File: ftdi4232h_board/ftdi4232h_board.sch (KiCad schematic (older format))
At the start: 20 parts

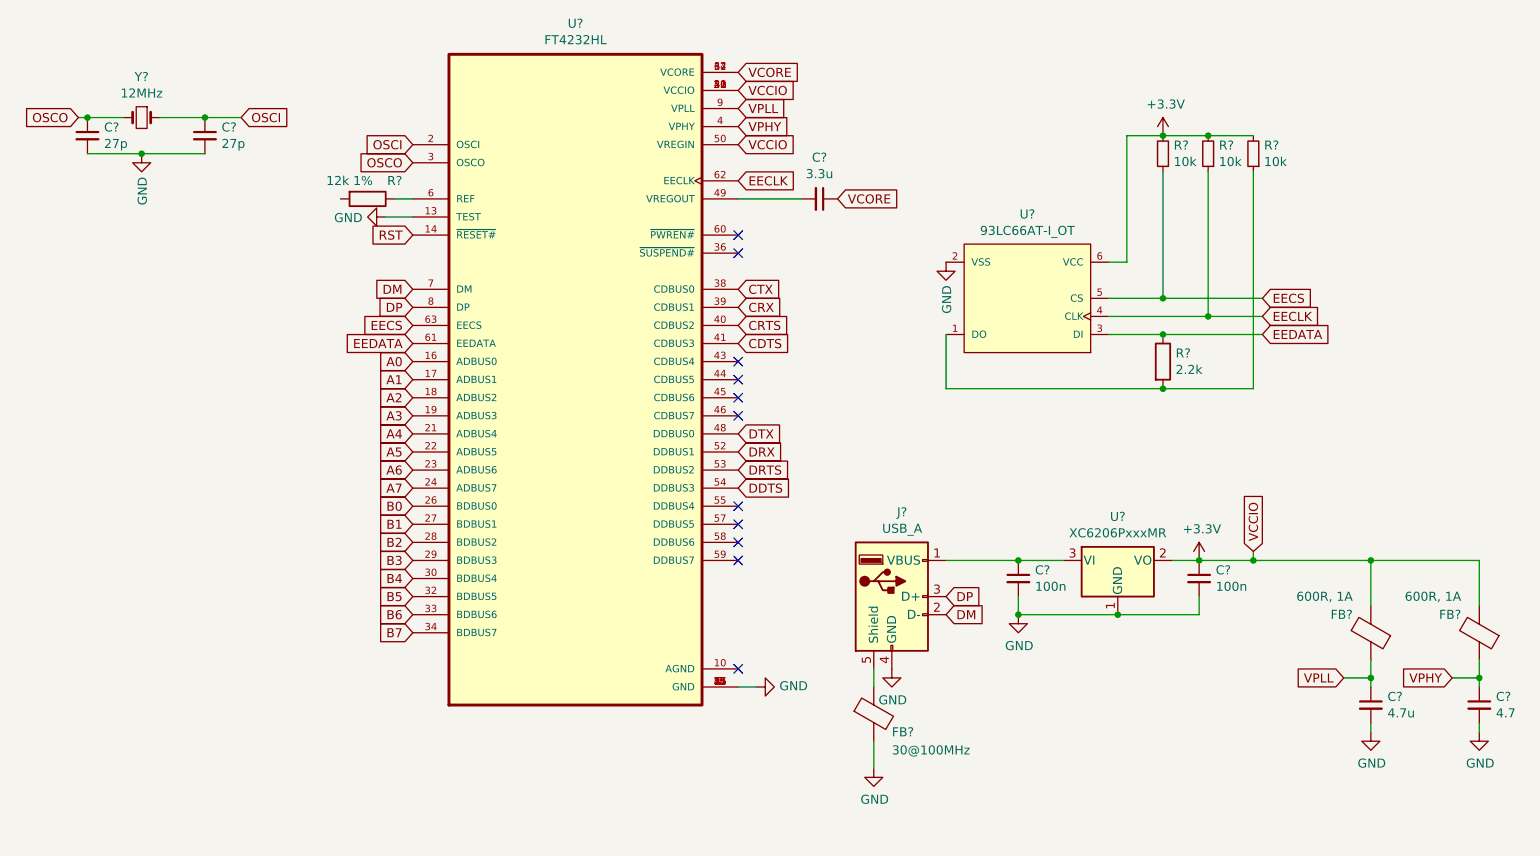
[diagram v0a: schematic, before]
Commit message: Use TPD2E2U06 as ESD protection for USB
The PCB design seems much more natural for USB using this IC compared to
alternatives.
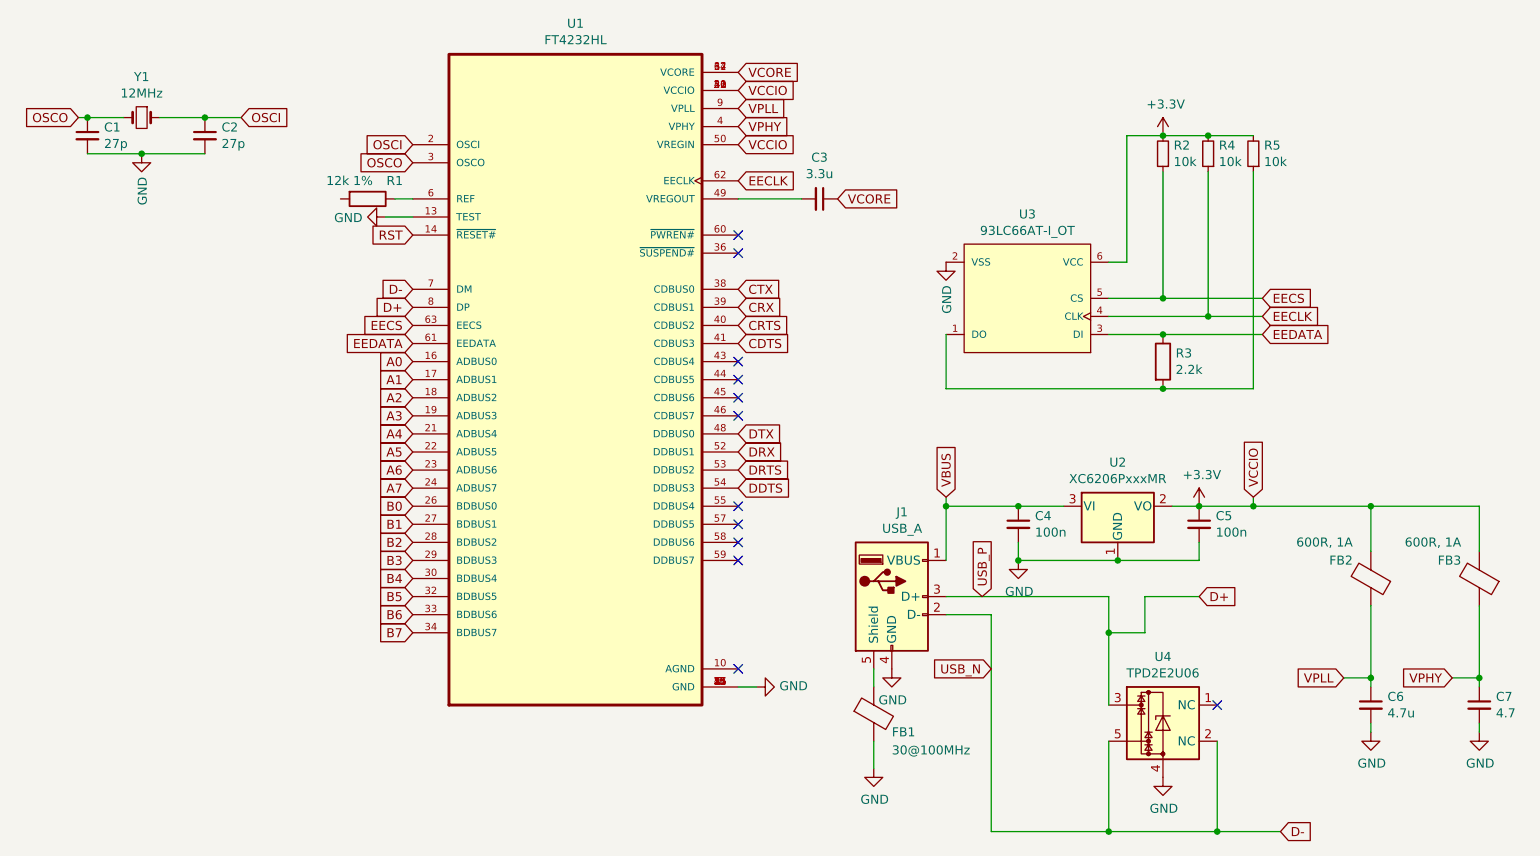
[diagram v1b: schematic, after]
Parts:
- added U4: TPD2E2U06, Package_TO_SOT_SMD:SOT-543, symbol Power_Protection:TPD2E2U06
- C1, C2, C3, C4, C5, C6, C7: renamed from C?; footprint (none) -> Capacitor_SMD:C_0603_1608Metric
- FB1, FB2, FB3: renamed from FB?; footprint (none) -> Inductor_SMD:L_0805_2012Metric
- J1: renamed from J?; footprint (none) -> Connector_USB:USB_A_Molex_105057_Vertical
- R1, R2, R3, R4, R5: renamed from R?; footprint (none) -> Resistor_SMD:R_0603_1608Metric
- U3: renamed from U?; footprint Microchip-93LC66AT-I_OT-* -> 93lc66at-iot:SOT95P280X145-6N
- Y1: renamed from Y?; footprint (none) -> Crystal:Crystal_SMD_3225-4Pin_3.2x2.5mm
- gave numbers to parts that had none: 2
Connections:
- net GND: now also U4.4
- net VBUS: now reaches C4.1, J1.1 (VBUS), U2.3 (VI)
- net DM renamed D-
- net D-: now also U4.2 (NC), U4.5
- net DP renamed D+
- net D+: now also U4.3
- no-connect marks 11 -> 12
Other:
- moved on the sheet: C4, C5, FB2, FB3, U2
